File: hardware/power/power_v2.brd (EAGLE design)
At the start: 92 x 92 mm, 61 parts, among them J1 FASTON1289_ST, J2 FASTON1289_ST, J3 12v, J4 5v, J5 XT30PW-F, J6 XT30PW-F, J7 XT30PW-F, J8 XT30PW-F, Q1 MMBT5401L, Q2 PSMN1R0-40YSH, Q3 MMBT5401L, Q4 PSMN1R0-40YSH, U1 PDQ30-Q24-S5-D, U2 PDQ30-Q24-S12-D

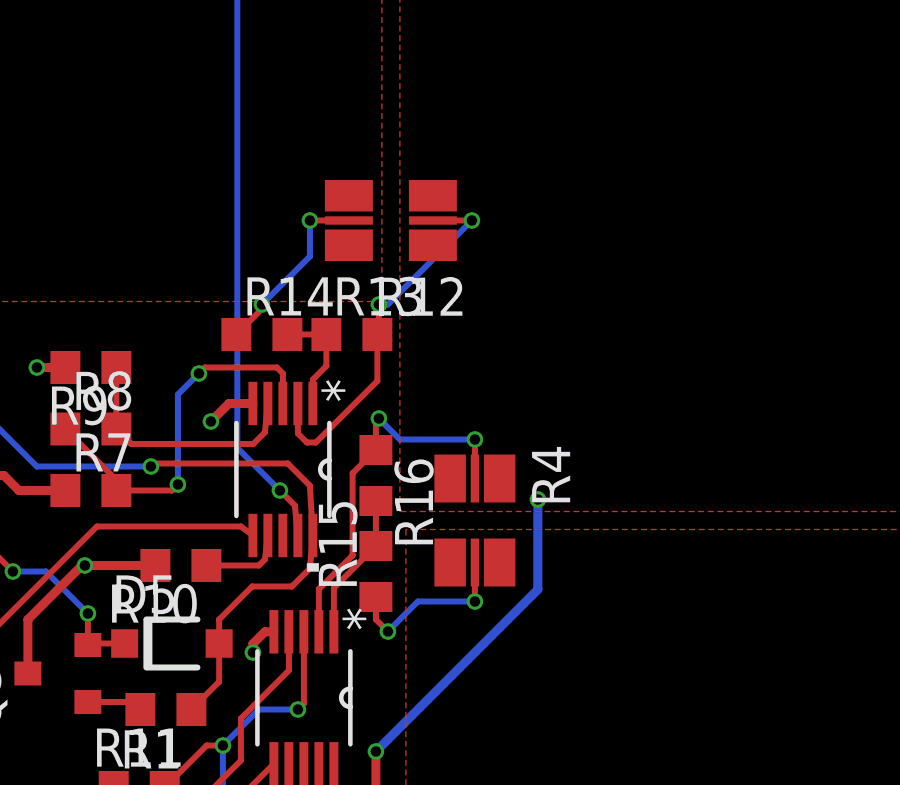
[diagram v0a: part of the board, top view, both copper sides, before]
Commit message: Reordered schematic
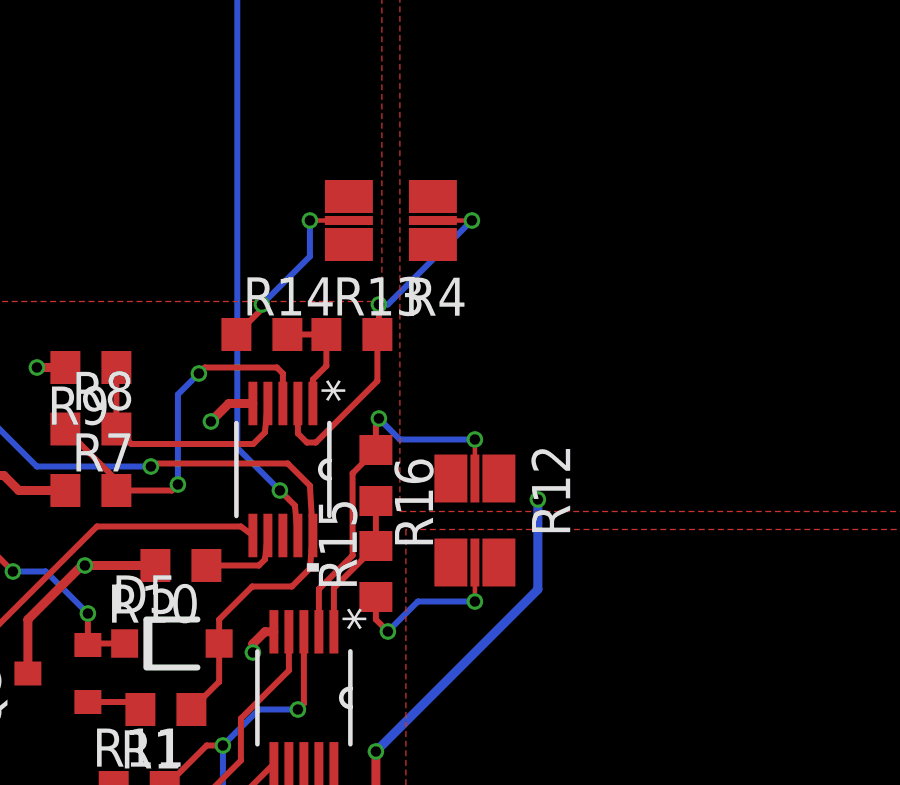
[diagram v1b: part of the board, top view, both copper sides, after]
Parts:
- R12, R4: value PMR25HZPFV -> PMR25HZPFV1L00
- moved R12 10.4 mm to (24.8, 38.1), turned to 270 degrees
- moved R4 10.4 mm to (22.0, 48.1), turned to 180 degrees
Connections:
- net +24V_LEG renamed +24V_POWER
- net MOSFET_DRAIN: now also R12.2A, R12.2B; no longer R4.2A, R4.2B
- net MOSFET_DRAIN1: now also R4.2A, R4.2B; no longer R12.2A, R12.2B
- net N$11: now also R12.2_KELVIN; no longer R4.2_KELVIN
- net N$19: now also R12.1_KELVIN; no longer R4.1_KELVIN
- net N$21: now also R4.2_KELVIN; no longer R12.2_KELVIN
- net N$22: now also R4.1_KELVIN; no longer R12.1_KELVIN
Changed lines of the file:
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@@
 <attribute name="VALUE" x="7.805" y="22.775" size="1.27" layer="27" rot="R180"/>
-</element>
-<element name="R4" library="timlib" library_urn="urn:adsk.eagle:library:16152524" package="R1210_KELVIN" package3d_urn="urn:adsk.eagle:package:16502583/2" value="PMR25HZPFV" x="24.8" y="38.1" smashed="yes" rot="R270">
-<attribute name="NAME" x="26.705" y="40.64" size="1.27" layer="25" rot="R270"/>
-<attribute name="VALUE" x="21.625" y="40.64" size="1.27" layer="27" rot="R270"/>
 </element>
 <element name="U$13" library="timlib" library_urn="urn:adsk.eagle:library:16152524" package="M80-8420242" package3d_urn="urn:adsk.eagle:package:16399492/3" value="2-PIN" x="18.3" y="11" smashed="yes"/>
@@
 <attribute name="VALUE" x="7.805" y="40.475" size="1.27" layer="27" rot="R180"/>
 </element>
-<element name="R12" library="timlib" library_urn="urn:adsk.eagle:library:16152524" package="R1210_KELVIN" package3d_urn="urn:adsk.eagle:package:16502583/2" value="PMR25HZPFV" x="22" y="48.1" smashed="yes" rot="R180">
-<attribute name="NAME" x="24.54" y="46.195" size="1.27" layer="25" rot="R180"/>
-<attribute name="VALUE" x="24.54" y="51.275" size="1.27" layer="27" rot="R180"/>
-</element>
 <element name="D3" library="timlib" library_urn="urn:adsk.eagle:library:16152524" package="SOD123" package3d_urn="urn:adsk.eagle:package:16502213/2" value="1N4148W-7-F" x="17.7" y="20.8" smashed="yes">
 <attribute name="NAME" x="15.7" y="21.8" size="1.27" layer="25"/>
@@
 <attribute name="SPICEPREFIX" value="R" x="21.5" y="39.6" size="1.778" layer="27" rot="R270" display="off"/>
 <attribute name="VALUE" x="19.595" y="40.235" size="1.27" layer="27" rot="R270"/>
+</element>
+<element name="R4" library="timlib" library_urn="urn:adsk.eagle:library:16152524" package="R1210_KELVIN" package3d_urn="urn:adsk.eagle:package:16502583/1" value="PMR25HZPFV1L00" x="22" y="48.1" smashed="yes" rot="R180">
+<attribute name="NAME" x="24.54" y="46.195" size="1.27" layer="25" rot="R180"/>
+<attribute name="VALUE" x="24.54" y="51.275" size="1.27" layer="27" rot="R180"/>
+</element>
+<element name="R12" library="timlib" library_urn="urn:adsk.eagle:library:16152524" package="R1210_KELVIN" package3d_urn="urn:adsk.eagle:package:16502583/1" value="PMR25HZPFV1L00" x="24.8" y="38.1" smashed="yes" rot="R270">
+<attribute name="NAME" x="26.705" y="40.64" size="1.27" layer="25" rot="R270"/>
+<attribute name="VALUE" x="21.625" y="40.64" size="1.27" layer="27" rot="R270"/>
 </element>
 </elements>
@@
 <contactref element="J1" pad="P$1"/>
 <contactref element="U$26" pad="1"/>
-<contactref element="R4" pad="1B"/>
-<contactref element="R4" pad="1A"/>
 <contactref element="U$13" pad="1"/>
-<contactref element="R12" pad="1B"/>
-<contactref element="R12" pad="1A"/>
 <polygon width="0.1524" layer="1" isolate="0.3" thermals="no" rank="2">
 <vertex x="60.6" y="61"/>
@@
 <wire x1="29.58" y1="12.02" x2="29.58" y2="11" width="0.3" layer="1"/>
 <wire x1="27.88" y1="9.3" x2="29.58" y2="11" width="0.3" layer="1"/>
+<contactref element="R4" pad="1A"/>
+<contactref element="R12" pad="1A"/>
+<contactref element="R4" pad="1B"/>
+<contactref element="R12" pad="1B"/>
 </signal>
 <signal name="GND_BATT">
@@
 <signal name="MOSFET_DRAIN">
 <contactref element="Q2" pad="5"/>
-<contactref element="R4" pad="2B"/>
-<contactref element="R4" pad="2A"/>
 <polygon width="0.1524" layer="1" isolate="0.3" thermals="no" rank="3">
 <vertex x="49.1" y="13"/>
@@
 <vertex x="22.5" y="13"/>
 </polygon>
+<contactref element="R12" pad="2A"/>
+<contactref element="R12" pad="2B"/>
 </signal>
 <signal name="N$5">
@@
 <wire x1="16.1" y1="27.99" x2="18.1" y2="29.99" width="0.2" layer="1"/>
 </signal>
-<signal name="+24V_LEG">
+<signal name="+24V_POWER">
 <contactref element="U$1" pad="9"/>
 <contactref element="D2" pad="C"/>
@@
 <signal name="MOSFET_DRAIN1">
 <contactref element="Q4" pad="5"/>
-<contactref element="R12" pad="2A"/>
-<contactref element="R12" pad="2B"/>
 <polygon width="0.1524" layer="1" isolate="0.3" thermals="no">
 <vertex x="2" y="61"/>
@@
 <vertex x="21.7" y="61"/>
 </polygon>
+<contactref element="R4" pad="2A"/>
+<contactref element="R4" pad="2B"/>
 </signal>
 <signal name="N$21">
 <contactref element="R14" pad="1"/>
-<contactref element="R12" pad="2_KELVIN"/>
-<wire x1="20.6" y1="48.1" x2="19.3" y2="48.1" width="0.2" layer="1"/>
 <via x="19.3" y="48.1" extent="1-16" drill="0.35"/>
 <wire x1="19.3" y1="48.1" x2="19.3" y2="46.9" width="0.2" layer="16"/>
@@
 <wire x1="17.7" y1="45.3" x2="17.7" y2="45.15" width="0.2" layer="1"/>
 <wire x1="17.7" y1="45.15" x2="16.85" y2="44.3" width="0.2" layer="1"/>
+<contactref element="R4" pad="2_KELVIN"/>
+<wire x1="19.3" y1="48.1" x2="20.6" y2="48.1" width="0.1524" layer="1"/>
 </signal>
 <signal name="N$22">
-<contactref element="R12" pad="1_KELVIN"/>
 <contactref element="R13" pad="2"/>
 <contactref element="U$14" pad="2"/>
-<wire x1="23.4" y1="48.1" x2="24.7" y2="48.1" width="0.2" layer="1"/>
 <via x="24.7" y="48.1" extent="1-16" drill="0.35"/>
 <wire x1="24.7" y1="48.1" x2="21.9" y2="45.3" width="0.2" layer="16"/>
@@
 <wire x1="21.55" y1="42.75" x2="21.55" y2="44.3" width="0.2" layer="1"/>
 <wire x1="19.5" y1="40.7" x2="21.55" y2="42.75" width="0.2" layer="1"/>
+<contactref element="R4" pad="1_KELVIN"/>
+<wire x1="24.7" y1="48.1" x2="23.4" y2="48.1" width="0.1524" layer="1"/>
 </signal>
 <signal name="N$10">
@@
 <signal name="N$11">
 <contactref element="R15" pad="1"/>
-<contactref element="R4" pad="2_KELVIN"/>
 <wire x1="21.5" y1="35.55" x2="21.5" y2="34.8" width="0.2" layer="1"/>
 <wire x1="21.5" y1="34.8" x2="21.9" y2="34.4" width="0.2" layer="1"/>
@@
 <wire x1="22.9" y1="35.4" x2="24.8" y2="35.4" width="0.2" layer="16"/>
 <via x="24.8" y="35.4" extent="1-16" drill="0.35"/>
-<wire x1="24.8" y1="35.4" x2="24.8" y2="36.7" width="0.2" layer="1"/>
+<contactref element="R12" pad="2_KELVIN"/>
+<wire x1="24.8" y1="35.4" x2="24.8" y2="36.7" width="0.1524" layer="1"/>
 </signal>
 <signal name="N$19">
-<contactref element="R4" pad="1_KELVIN"/>
 <contactref element="R16" pad="1"/>
 <contactref element="U$1" pad="2"/>
-<wire x1="24.8" y1="39.5" x2="24.8" y2="40.8" width="0.2" layer="1"/>
 <via x="24.8" y="40.8" extent="1-16" drill="0.35"/>
 <wire x1="24.8" y1="40.8" x2="22.3" y2="40.8" width="0.2" layer="16"/>
@@
 <wire x1="19.6" y1="34.39" x2="19.6" y2="35.81245" width="0.2" layer="1"/>
 <wire x1="19.6" y1="35.81245" x2="20.723" y2="36.93545" width="0.2" layer="1"/>
+<contactref element="R12" pad="1_KELVIN"/>
+<wire x1="24.8" y1="40.8" x2="24.8" y2="39.5" width="0.1524" layer="1"/>
 </signal>
 </signals>

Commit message: Updates to power board
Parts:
- removed C23: 10uF, timlib:C1210
- removed U$13, U$26: 2-PIN, timlib:M80-8420242
- added C11: 2.2nF, rcl:C0603
- added H1, H2, H3, H4, H5, H6: GND_HOLE_M3, timlib:HOLE_GND_M3
- added J100, J101: FASTON1289_ST, timlib:FASTON_1289-ST
- C1, C2, C3, C4, C5, C6, C7: value 220uf -> 10uF; device timlib:C_ELEC_8X11_5 -> timlib:C1210
- C10: value 16nF -> 10uF
- C12: value 2.2n -> 0.01uF
- C13: value 16nF -> 47nF; device timlib:C1210 -> rcl:C0603
- C14: value 10uF -> 2.2nF; device timlib:C1210 -> rcl:C0603
- C15, C17, C18, C19, C20, C21, C22: value 10uF -> 220uf; device timlib:C1210 -> timlib:C_ELEC_8X11_5
- C16: value 10uF -> 47nF; device timlib:C1210 -> rcl:C0603
- C8: value 0.01uF -> 2.2nF
- C9: value 2.2n -> 10uF
- D1: value SMAJ30A -> SK510A-LTP
- D2: value SK510A-LTP -> SMAJ30A
- D4: value SK510A-LTP -> 1N4148W-7-F; device timlib:DO-214AC -> timlib:SOD123
- D5: value 1N4148W-7-F -> SK510A-LTP; device timlib:SOD123 -> timlib:DO-214AC
- J1: value FASTON1289_ST -> 12v; device timlib:FASTON_1289-ST -> timlib:MOLEX_4_RA
- J2: value FASTON1289_ST -> 5v; device timlib:FASTON_1289-ST -> timlib:MOLEX_4_RA
- J3: value 12v -> XT30PW-F; device timlib:MOLEX_4_RA -> timlib:XT30PW-F
- J4: value 5v -> XT30PW-F; device timlib:MOLEX_4_RA -> timlib:XT30PW-F
- J7, J8: value XT30PW-F -> 2-PIN; device timlib:XT30PW-F -> timlib:M80-8420242
- Q1: value MMBT5401L -> PSMN1R0-40YSH; device timlib:SOT23-3 -> timlib:LFPAK56E
- Q2: value PSMN1R0-40YSH -> MMBT5401L; device timlib:LFPAK56E -> timlib:SOT23-3
- R1: value 47.5k -> 4.32k
- R10: value 18.9k -> 3.4k
- R11: value 18.9 -> 1k
- R12: value PMR25HZPFV1L00 -> 18.9k; device timlib:R1210_KELVIN -> rcl:R0603
- R13: value 10 -> 18.9k
- R15: value 4.53 -> 4.32k
- R16: value 10 -> 1k
- R3, R9: value 4.32k -> 47.5k
- R4: value PMR25HZPFV1L00 -> 4.53; device timlib:R1210_KELVIN -> rcl:R0603
- R5: value 18.9k -> 10
- R6: value 18.9 -> 10
- R7: value 47.5k -> 0.002; device rcl:R0603 -> timlib:R1210_KELVIN
- R8: value 3.4k -> 0.002; device rcl:R0603 -> timlib:R1210_KELVIN
- U1: value PDQ30-Q24-S5-D -> PDQ30-Q24-S12-D
- U2: value PDQ30-Q24-S12-D -> PDQ30-Q24-S5-D
- moved C22 99.4 mm to (69.7, 7.26), turned to 270 degrees
- moved C21 92.3 mm to (60.9, 7.26), turned to 270 degrees
- moved C3 91.0 mm to (9.36, 82.3), turned to 90 degrees
- moved C6 91.0 mm to (19.6, 83.2), turned to 0 degrees
- moved C20 89.0 mm to (69.7, 15.6), turned to 270 degrees
- moved C2 86.1 mm to (6.32, 82.3), turned to 90 degrees
- moved C1 83.1 mm to (3.28, 82.3), turned to 90 degrees
- moved C17 83.0 mm to (60.9, 24.0), turned to 270 degrees
- moved C4 82.4 mm to (12.4, 82.3), turned to 90 degrees
- moved C7 81.7 mm to (19.6, 80.2), turned to 0 degrees
- moved C5 73.9 mm to (15.4, 82.3), turned to 90 degrees
- moved C19 71.9 mm to (69.7, 24.0), turned to 270 degrees
- moved D5 71.4 mm to (80.3, 5.75)
- moved C18 70.3 mm to (60.9, 15.6), turned to 270 degrees
- moved C15 70.3 mm to (69.7, 32.4), turned to 270 degrees
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- renumbered U$1 to U3, U$14 to U4
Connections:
- net +12VOUT: now also J1.CIRCUIT2, J1.CIRCUIT4, U1.P$3; no longer J3.CIRCUIT2, J3.CIRCUIT4, U2.P$3
- net +24V_BATT: now also C12.1, D2.C, J101.P$1, J101.P$2, J7.1, J8.1, R7.1A, R7.1B, R8.1A, R8.1B; no longer C8.1, D1.C, J1.P$1, J1.P$2, R12.1A, R12.1B, R4.1A, R4.1B, U$13.1, U$26.1
- net +24V_ISO: now also C1.1, C10.1, C2.1, C3.1, C4.1, C5.1, C6.1, C7.1, C8.1, C9.1, D1.C, Q1.1, Q1.2, Q1.3; no longer C14.1, C15.1, C16.1, C17.1, C18.1, C19.1, C20.1, C21.1, C22.1, C23.1, D4.C, Q4.1, Q4.2, Q4.3
- net +24V_POWER: now also C15.1, C17.1, C18.1, C19.1, C20.1, C21.1, C22.1, D5.C, J3.P$2, J4.P$2, Q4.1, Q4.2, Q4.3; no longer C1.1, C2.1, C3.1, C4.1, C5.1, C6.1, C7.1, D2.C, J7.P$2, J8.P$2, Q2.1, Q2.2, Q2.3
- net +5VOUT: now also J2.CIRCUIT2, J2.CIRCUIT4, U2.P$3; no longer J4.CIRCUIT2, J4.CIRCUIT4, U1.P$3
- net 12V_GND: now also J1.CIRCUIT1, J1.CIRCUIT3, U1.P$5; no longer J3.CIRCUIT1, J3.CIRCUIT3, U2.P$5
- net 5V_GND: now also J2.CIRCUIT1, J2.CIRCUIT3, U2.P$5; no longer J4.CIRCUIT1, J4.CIRCUIT3, U1.P$5
- net GND_BATT: now also C11.2, D5.A, H1.P$1, H2.P$1, H3.P$1, H4.P$1, H5.P$1, H6.P$1, J100.P$1, J100.P$2, J3.P$1, J4.P$1, Q2.C, R1.2, R12.2, R13.2, R15.2; no longer C23.2, D4.A, J2.P$1, J2.P$2, J7.P$1, J8.P$1, Q1.C, R10.2, R3.2, R5.2, R9.2
- net MOSFET_DRAIN: now also Q4.5, R8.2A, R8.2B; no longer Q2.5, R12.2A, R12.2B
- net MOSFET_DRAIN1: now also Q1.5, R7.2A, R7.2B; no longer Q4.5, R4.2A, R4.2B
- net N$1: now also R10.1, R9.2; no longer R1.2, R2.1
- net N$10: now also R14.2, R6.2; no longer R15.2, R16.2
- net N$11: now also R14.1, R8.2_KELVIN; no longer R12.2_KELVIN, R15.1
- net N$12: now also R1.1, R2.2; no longer R8.2, R9.1
- net N$13: now also J7.2, R3.1; no longer R7.1, U$13.2
- net N$14: now also D3.A, Q1.4; no longer D5.A, Q4.4
- net N$15: now also R12.1; no longer R10.1
- net N$16: now also C11.1; no longer C12.1
- net N$17: now also D3.C, Q2.E; no longer D5.C, Q3.E
- net N$18: now also Q2.B; no longer Q3.B
- net N$19: now also R6.1, R8.1_KELVIN; no longer R12.1_KELVIN, R16.1
- net N$2: now also R10.2, R15.1; no longer R2.2, R3.1
- net N$20: now also R4.2, R5.1; no longer R13.1, R14.2
- net N$21: now also R4.1, R7.2_KELVIN; no longer R14.1, R4.2_KELVIN
- net N$22: now also R5.2, R7.1_KELVIN; no longer R13.2, R4.1_KELVIN
- net N$3: now also J8.2, R9.1; no longer R1.1, U$26.2
- net N$4: now also R2.1, R3.2; no longer R7.2, R8.1
- net N$5: now also D4.A, Q4.4, R16.1; no longer D3.A, Q2.4, R6.1
- net N$6: now also R13.1; no longer R5.1
- net N$7: now also C14.1; no longer C9.1
- net N$8: now also C16.1, D4.C, Q3.E; no longer C10.1, D3.C, Q1.E
- net N$9: now also Q3.B, R16.2; no longer Q1.B, R6.2
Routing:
- net N$5: track 43.3 -> 64.5 mm, vias 2 -> 0
- net +24V_POWER: track 32.1 -> 47.5 mm
- net GND_BATT: track 17.6 -> 2.37 mm, vias 87 -> 7
- net N$7: track 15.6 -> 3.20 mm
- net N$16: track 11.8 -> 1.76 mm
- net +24V_BATT: track 49.1 -> 41.5 mm, vias 2 -> 3
- net N$8: track 9.32 -> 3.20 mm
- net N$13: track 35.8 -> 40.6 mm, vias 2 -> 0
- net N$17: track 7.85 -> 3.52 mm, vias 2 -> 0
- net N$4: track 12.8 -> 10.4 mm
- net N$3: track 31.6 -> 30.5 mm, vias 2 -> 0
- net N$1: track 12.7 -> 13.5 mm, vias 3 -> 2
- net 5V_GND: track 18.7 -> 18.2 mm
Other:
- board text added: "24V Power Breakout r1 Tim Blakely timblakely.com"
